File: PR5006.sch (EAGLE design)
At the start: 37 parts

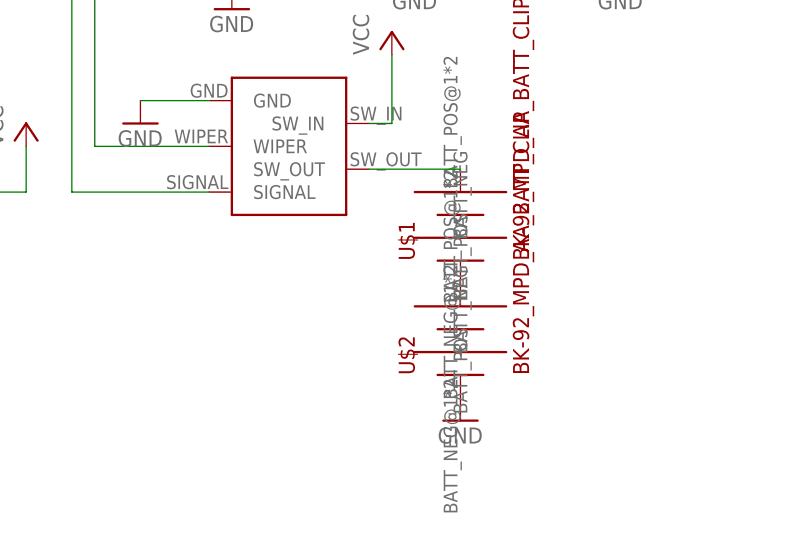
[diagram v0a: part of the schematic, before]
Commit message: Added Decoupling Cap
Final revisions
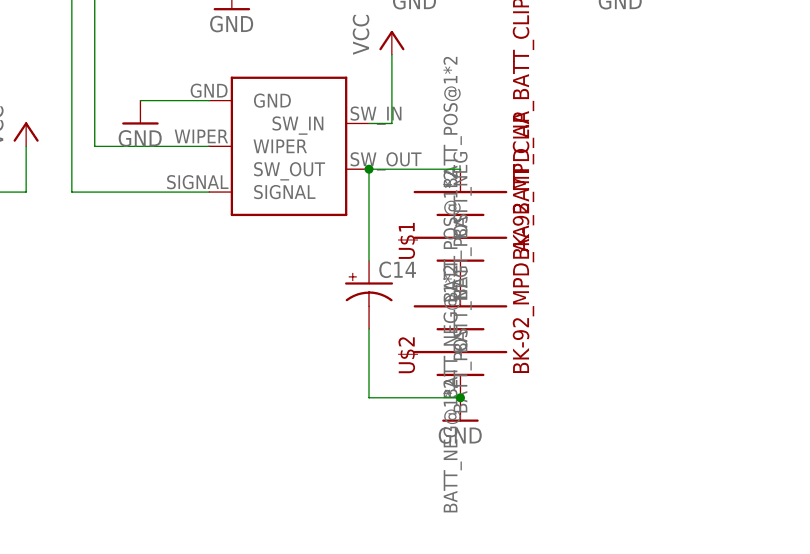
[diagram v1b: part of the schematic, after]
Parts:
- added C14: (no value), rcl:CPOL-USSANYO_C
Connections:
- removed net N$22: U$1.BATT_POS, U$5.SW_OUT
- new net N$32: C14.+, U$1.BATT_POS, U$5.SW_OUT
- net GND: now also C14.-
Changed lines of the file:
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@@
 <part name="U$1" library="PR_Libraries" deviceset="BK-92_MPD_AA_BATT_CLIP" device=""/>
 <part name="U$2" library="PR_Libraries" deviceset="BK-92_MPD_AA_BATT_CLIP" device=""/>
+<part name="C14" library="rcl" deviceset="CPOL-US" device="SANYO_C"/>
 </parts>
 <sheets>
@@
 <instance part="U$1" gate="G$1" x="137.16" y="45.72" rot="R90"/>
 <instance part="U$2" gate="G$1" x="137.16" y="33.02" rot="R90"/>
+<instance part="C14" gate="G$1" x="127" y="38.1"/>
 </instances>
 <busses>
@@
 <pinref part="U$2" gate="G$1" pin="BATT_NEG"/>
 <pinref part="GND14" gate="1" pin="GND"/>
+<wire x1="127" y1="33.02" x2="127" y2="25.4" width="0.1524" layer="91"/>
+<wire x1="127" y1="25.4" x2="137.16" y2="25.4" width="0.1524" layer="91"/>
+<junction x="137.16" y="25.4"/>
+<pinref part="C14" gate="G$1" pin="-"/>
 </segment>
 </net>
@@
 </segment>
 </net>
-<net name="N$22" class="0">
-<segment>
-<pinref part="U$5" gate="G$1" pin="SW_OUT"/>
-<wire x1="137.16" y1="50.8" x2="127" y2="50.8" width="0.1524" layer="91"/>
-<pinref part="U$1" gate="G$1" pin="BATT_POS"/>
-</segment>
-</net>
 <net name="N$5" class="0">
 <segment>
@@
 </segment>
 </net>
+<net name="N$32" class="0">
+<segment>
+<pinref part="U$5" gate="G$1" pin="SW_OUT"/>
+<wire x1="137.16" y1="50.8" x2="127" y2="50.8" width="0.1524" layer="91"/>
+<pinref part="U$1" gate="G$1" pin="BATT_POS"/>
+<wire x1="127" y1="40.64" x2="127" y2="50.8" width="0.1524" layer="91"/>
+<junction x="127" y="50.8"/>
+<pinref part="C14" gate="G$1" pin="+"/>
+</segment>
+</net>

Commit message: more stuff post todd
new thru hole cap on tune circuit, different restrict zone around
antenna… etc
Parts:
- C1: device resistor:C-USC0603 -> resistor:CPOL-USE2-5
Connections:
- net GND: now also C1.-; no longer C1.2
- net N$21: now also C1.+; no longer C1.1
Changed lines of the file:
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@@
 <?xml version="1.0" encoding="utf-8"?>
 <!DOCTYPE eagle SYSTEM "eagle.dtd">
-<eagle version="6.4">
+<eagle version="6.5.0">
 <drawing>
 <settings>
@@
 <part name="R3" library="resistor" deviceset="R-US_" device="R0603" value="1K"/>
 <part name="R1" library="resistor" deviceset="R-US_" device="R0603" value="412K"/>
-<part name="C1" library="resistor" deviceset="C-US" device="C0603" value="47uF"/>
+<part name="C1" library="resistor" deviceset="CPOL-US" device="E2-5" value="47uF"/>
 <part name="C2" library="resistor" deviceset="C-US" device="C0603" value=".1uF"/>
 <part name="GND13" library="SparkFun-Aesthetics" deviceset="GND" device=""/>
@@
 <segment>
 <pinref part="C2" gate="G$1" pin="2"/>
-<pinref part="C1" gate="G$1" pin="2"/>
+<pinref part="C1" gate="G$1" pin="-"/>
 <wire x1="-33.02" y1="76.2" x2="-38.1" y2="76.2" width="0.1524" layer="91"/>
 <pinref part="GND13" gate="1" pin="GND"/>
@@
 <segment>
 <pinref part="C2" gate="G$1" pin="1"/>
-<pinref part="C1" gate="G$1" pin="1"/>
+<pinref part="C1" gate="G$1" pin="+"/>
 <wire x1="-33.02" y1="83.82" x2="-35.56" y2="83.82" width="0.1524" layer="91"/>
 <wire x1="-40.64" y1="83.82" x2="-35.56" y2="83.82" width="0.1524" layer="91"/>

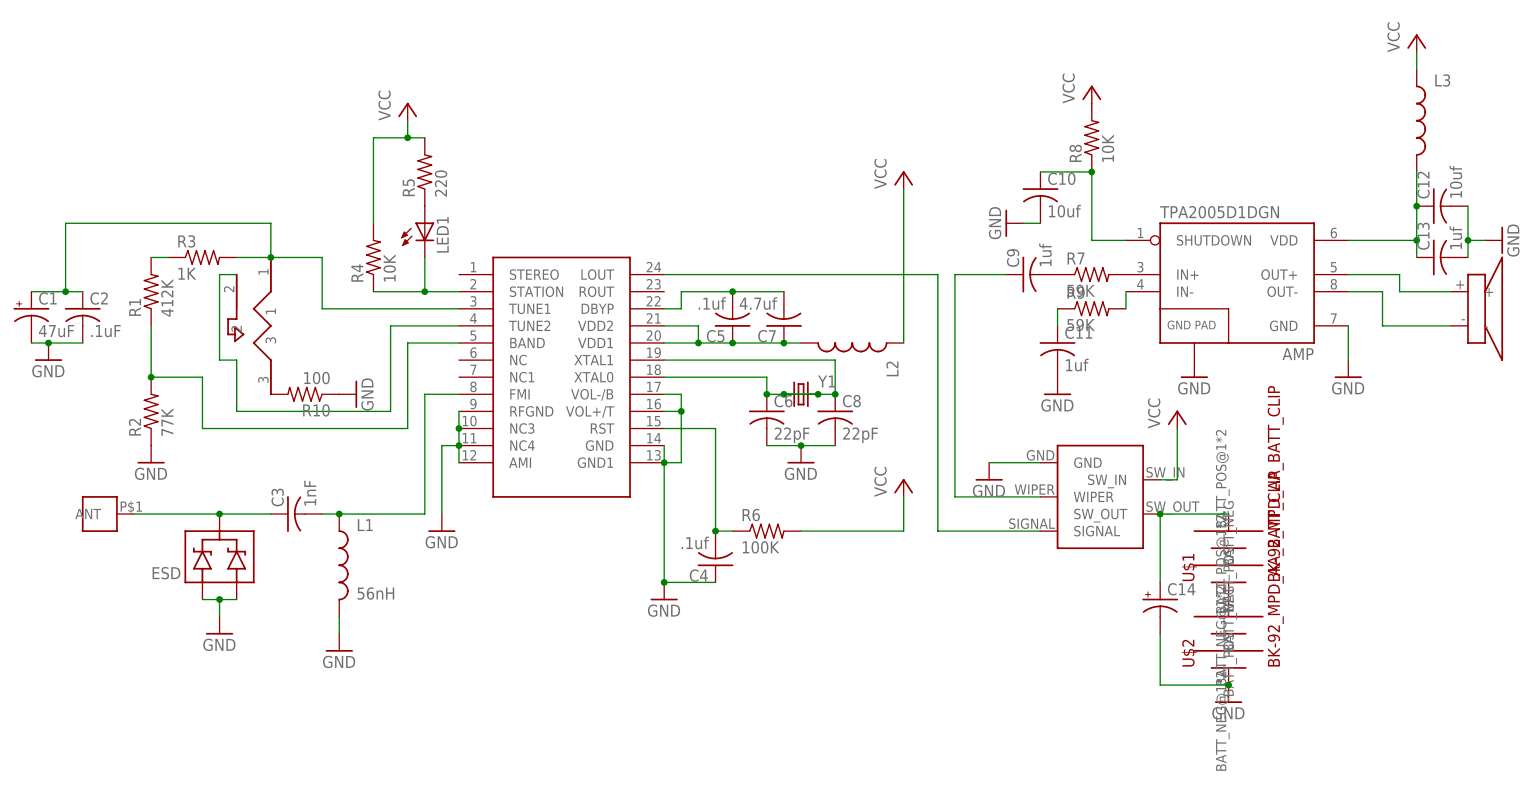
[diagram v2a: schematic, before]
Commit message: v1.4 initial commit
revised trimpot package. revised much layout stuff. added BMP.
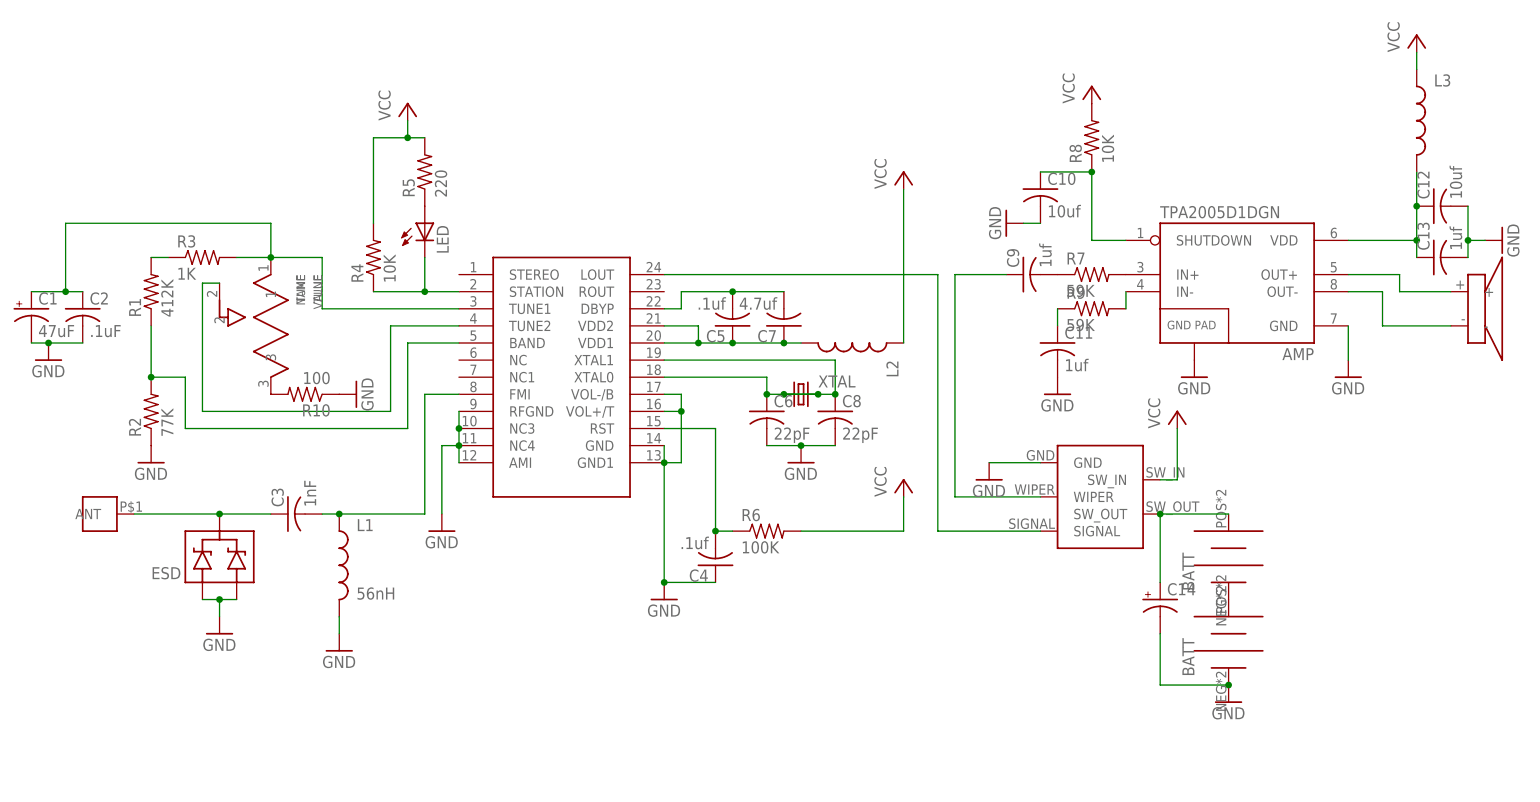
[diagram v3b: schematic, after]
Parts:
- removed U$6: (no value), PRTrimmer:BI-25XR_TRIMMER
- added TUNE: TUNE, PR_Libraries:64XR_BOURNS_TRIMPOT
- C1: device resistor:CPOL-USE2-5 -> resistor-copy:CPOL-USE2-5
- C14: device rcl:CPOL-USSANYO_C -> resistor-copy:CPOL-USE2.5-5
- renumbered LED1 to LED, SI1 to SI4831, Y1 to XTAL
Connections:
- net GND: now also U$2.NEG; no longer U$2.BATT_NEG
- net N$12: now also TUNE.2; no longer U$6.2
- net N$14: now also U$1.NEG, U$2.POS; no longer U$1.BATT_NEG, U$2.BATT_POS
- net N$21: now also TUNE.1; no longer U$6.1
- net N$29: now also TUNE.3; no longer U$6.3
- net N$32: now also U$1.POS; no longer U$1.BATT_POS
